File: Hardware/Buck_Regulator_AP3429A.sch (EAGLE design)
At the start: 8 parts

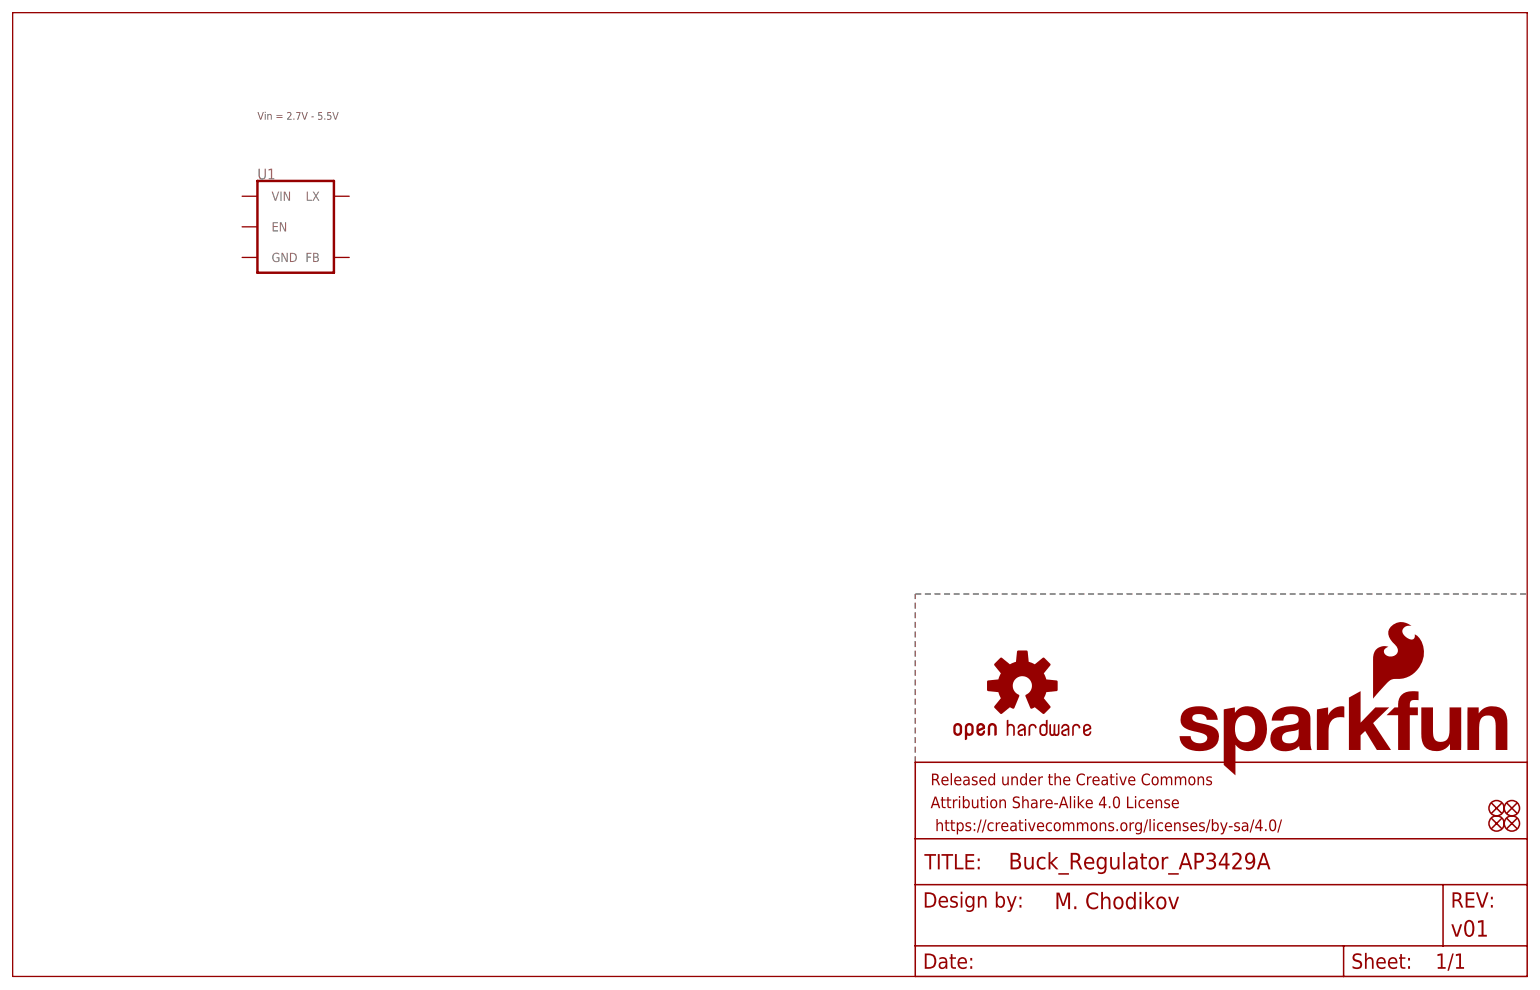
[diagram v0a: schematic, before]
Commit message: Addition of App Note, Updates to Schematic
Added connectors, power led, and main ic circuit with correctly rated components. The application note was added for the new product that Diodes Inc. sells, but it is the same exact part as the AP3429A but with a lower current limit (from 2A to 1A)
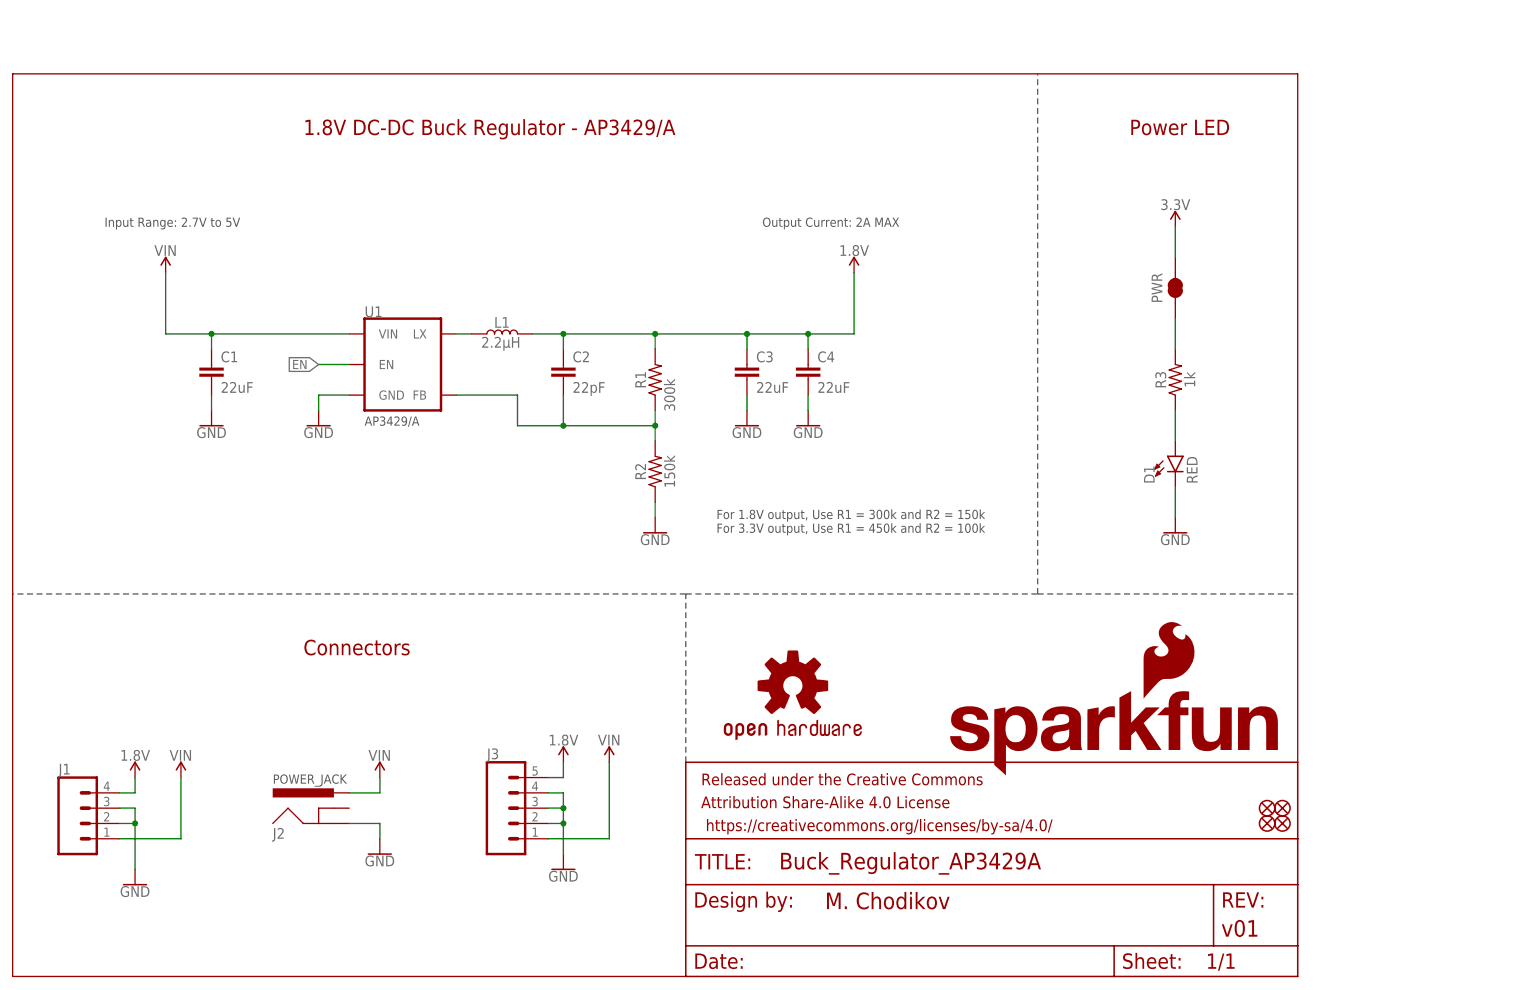
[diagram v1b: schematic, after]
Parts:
- added C1, C3, C4: 22uF, SparkFun-Capacitors:22UF-0603-6.3V-20%
- added C2: 22pF, SparkFun-Capacitors:22PF-0603-50V-5%
- added D1: RED, SparkFun-LED:LED-RED0603
- added J1: (no value), SparkFun-Connectors:CONN_04SCREW_LOCK
- added J2: POWER_JACKPOWER_JACK_SLOT, SparkFun-Connectors:POWER_JACKPOWER_JACK_SLOT
- added J3: (no value), SparkFun-Connectors:CONN_05
- added L1: 2.2μH, SparkFun-Coils:2.2μH-4X4-2.2μH-3A-45MOHM
- added PWR: JUMPER-SMT_2_NC_TRACE_SILK, SparkFun-Jumpers:JUMPER-SMT_2_NC_TRACE_SILK
- added R1: 300k, SparkFun-Resistors:300KOHM-0603-1/10W-1%
- added R2: 150k, SparkFun-Resistors:150KOHM-0603-1/10W-1%
- added R3: 1k, SparkFun-Resistors:1KOHM-0603-1/10W-1%
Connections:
- new net 1.8V: C2.1, C3.1, C4.1, J1.4, J3.5, L1.2, R1.2
- new net 3.3V: PWR.2
- new net EN: U1.EN
- new net GND: C1.2, C3.2, C4.2, D1.C, J2.GND, R2.1, U1.GND
- new net N$1: L1.1, U1.LX
- new net N$2: C2.2, R1.1, R2.2, U1.FB
- new net N$3: PWR.1, R3.2
- new net N$4: D1.A, R3.1
- new net N$6: J3.2, J3.3, J3.4
- new net N$7: J1.2, J1.3
- new net VIN: C1.1, J1.1, J2.PWR, J3.1, U1.VIN
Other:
- note added: "1.8V DC-DC Buck Regulator - AP3429/A"
- note added: "AP3429/A"
- note added: "Connectors"
- note added: "For 1.8V output, Use R1 = 300k and R2 = 150k For 3.3V output, Use R1 = 450k and R2 = 100k"
- note added: "Input Range: 2.7V to 5V"
- note added: "Output Current: 2A MAX"
- note added: "POWER_JACK"
- note added: "Power LED"
- note removed: "Vin = 2.7V - 5.5V"
- moved on the sheet: U1

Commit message: Update Buck_Regulator_AP3429A.sch
Attributes added for parts missing that information, finished first draft of initial schematic for 1.8V output, added further notation on what to change for 3.3V output instead of the 1.8V output.
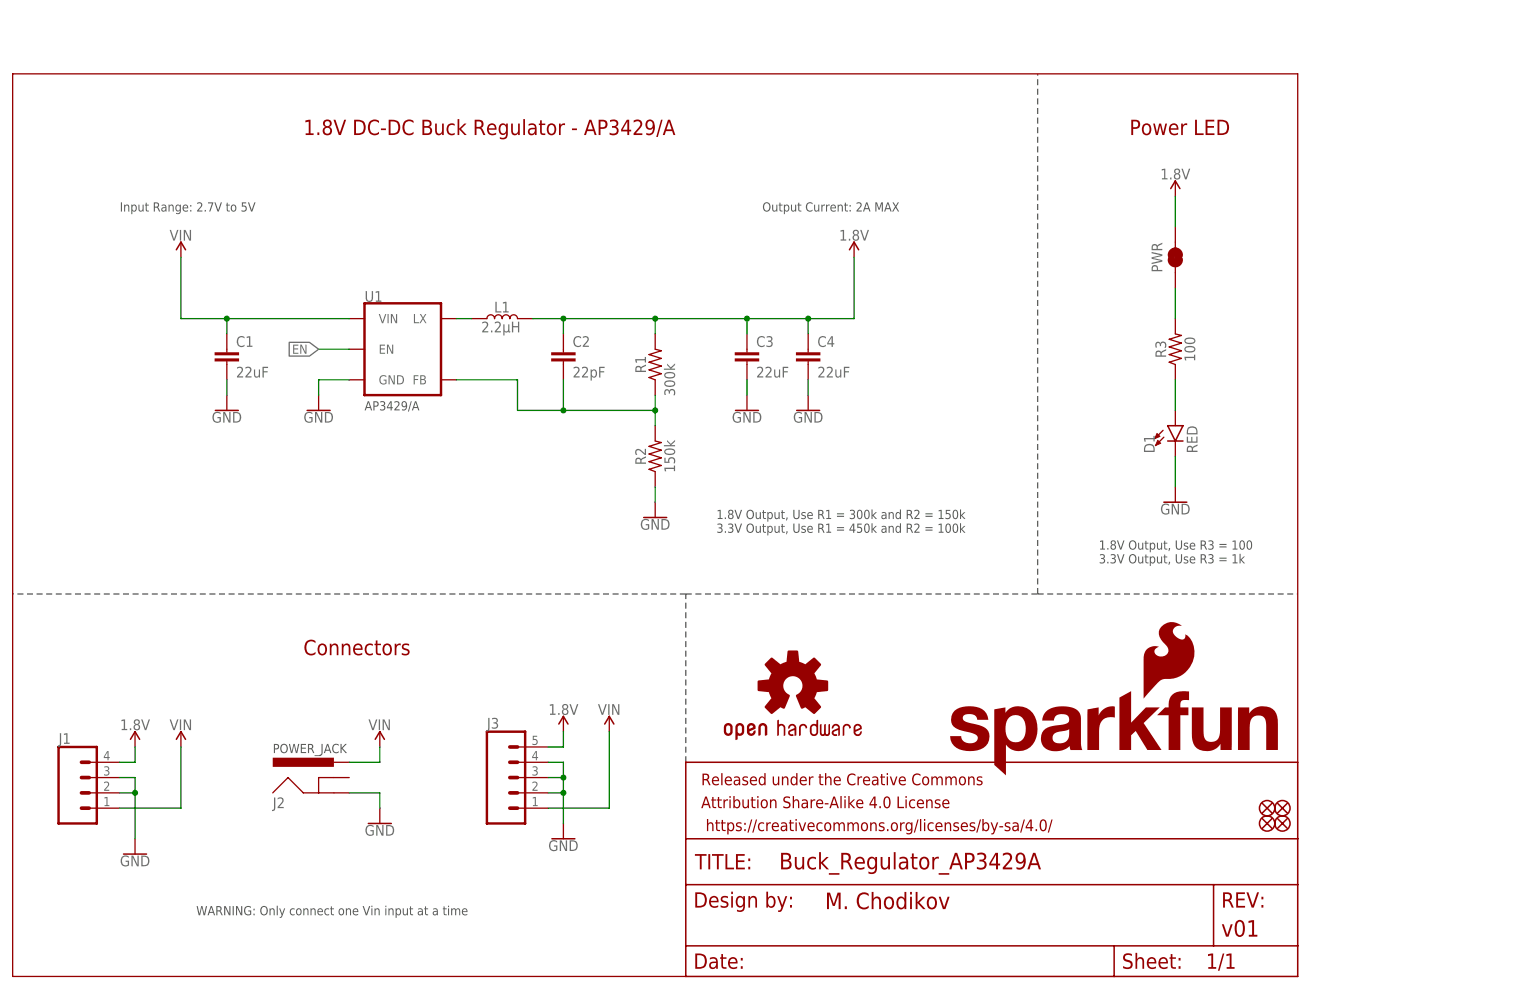
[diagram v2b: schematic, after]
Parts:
- C2: device SparkFun-Capacitors:22PF-0603-50V-5% -> SparkFun-Capacitors:22PF-0402T-16V-10%
- J1: PROD_ID (none) -> CONN-14485
- R3: value 1k -> 100; device SparkFun-Resistors:1KOHM-0603-1/10W-1% -> SparkFun-Resistors:100OHM-0603-1/10W-1%
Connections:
- removed net 3.3V: PWR.2
- net 1.8V: now also PWR.2
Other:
- note added: "1.8V Output, Use R1 = 300k and R2 = 150k 3.3V Output, Use R1 = 450k and R2 = 100k"
- note added: "1.8V Output, Use R3 = 100 3.3V Output, Use R3 = 1k"
- note added: "WARNING: Only connect one Vin input at a time"
- note removed: "For 1.8V output, Use R1 = 300k and R2 = 150k For 3.3V output, Use R1 = 450k and R2 = 100k"
- moved on the sheet: C1, C2, C3, C4, D1, J1, J2, J3, L1, PWR, R1, R2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

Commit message: Created Board file and cleaned up schematic
Added notation jumpers for 3.3V or 1.8V board, created board file and adjusted components to fit onto the board in a 1x1 form factor.
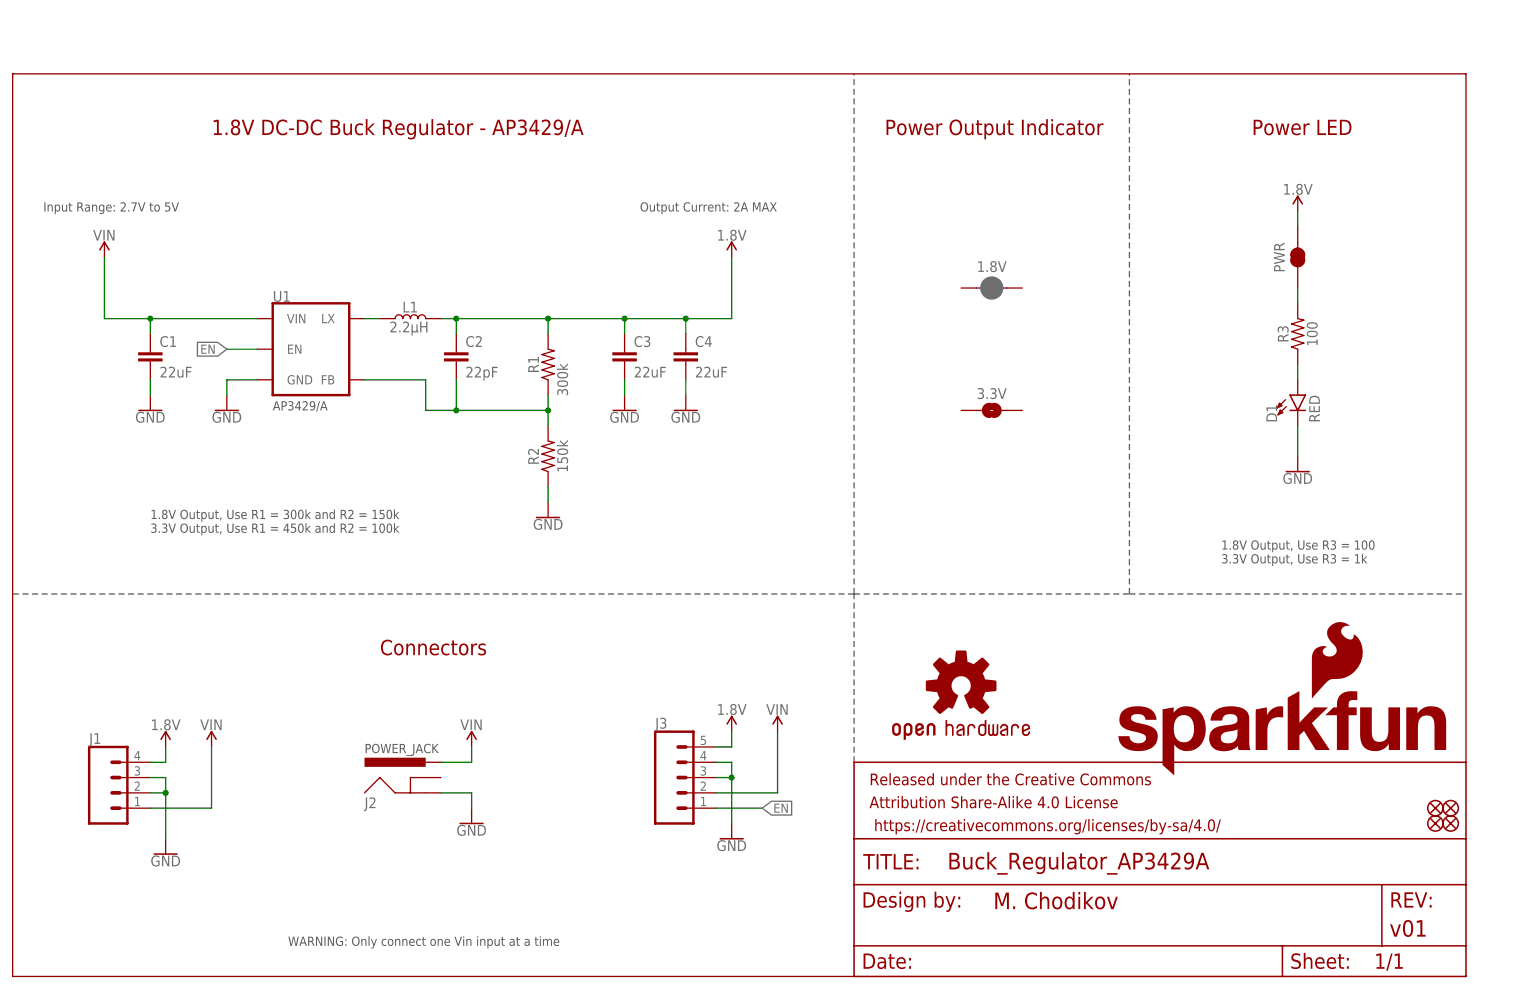
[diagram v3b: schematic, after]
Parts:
- added 1.8V: JUMPER-SMT_2_NC_PASTE_NO-SILK, SparkFun-Jumpers:JUMPER-SMT_2_NC_PASTE_NO-SILK
- added 3.3V: JUMPER-SMT_2_NO_NO-SILK, SparkFun-Jumpers:JUMPER-SMT_2_NO_NO-SILK
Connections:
- net EN: now also J3.1
- net N$6: no longer J3.2
- net VIN: now also J3.2; no longer J3.1
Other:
- note added: "Power Output Indicator"
- moved on the sheet: C1, C2, C3, C4, D1, J1, J2, J3, L1, PWR, R1, R2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

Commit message: Updates to project
Schematic: Changed indicator pads for soldering which version of board, added further notation, updated Power Jack device in local library.
Layout: Added power polygons and stitching vias to appropriate areas, finished routing, adjusted Power Jack to be double sided now, fixed silkscreen notation, adjusted version number, worked through design errors.
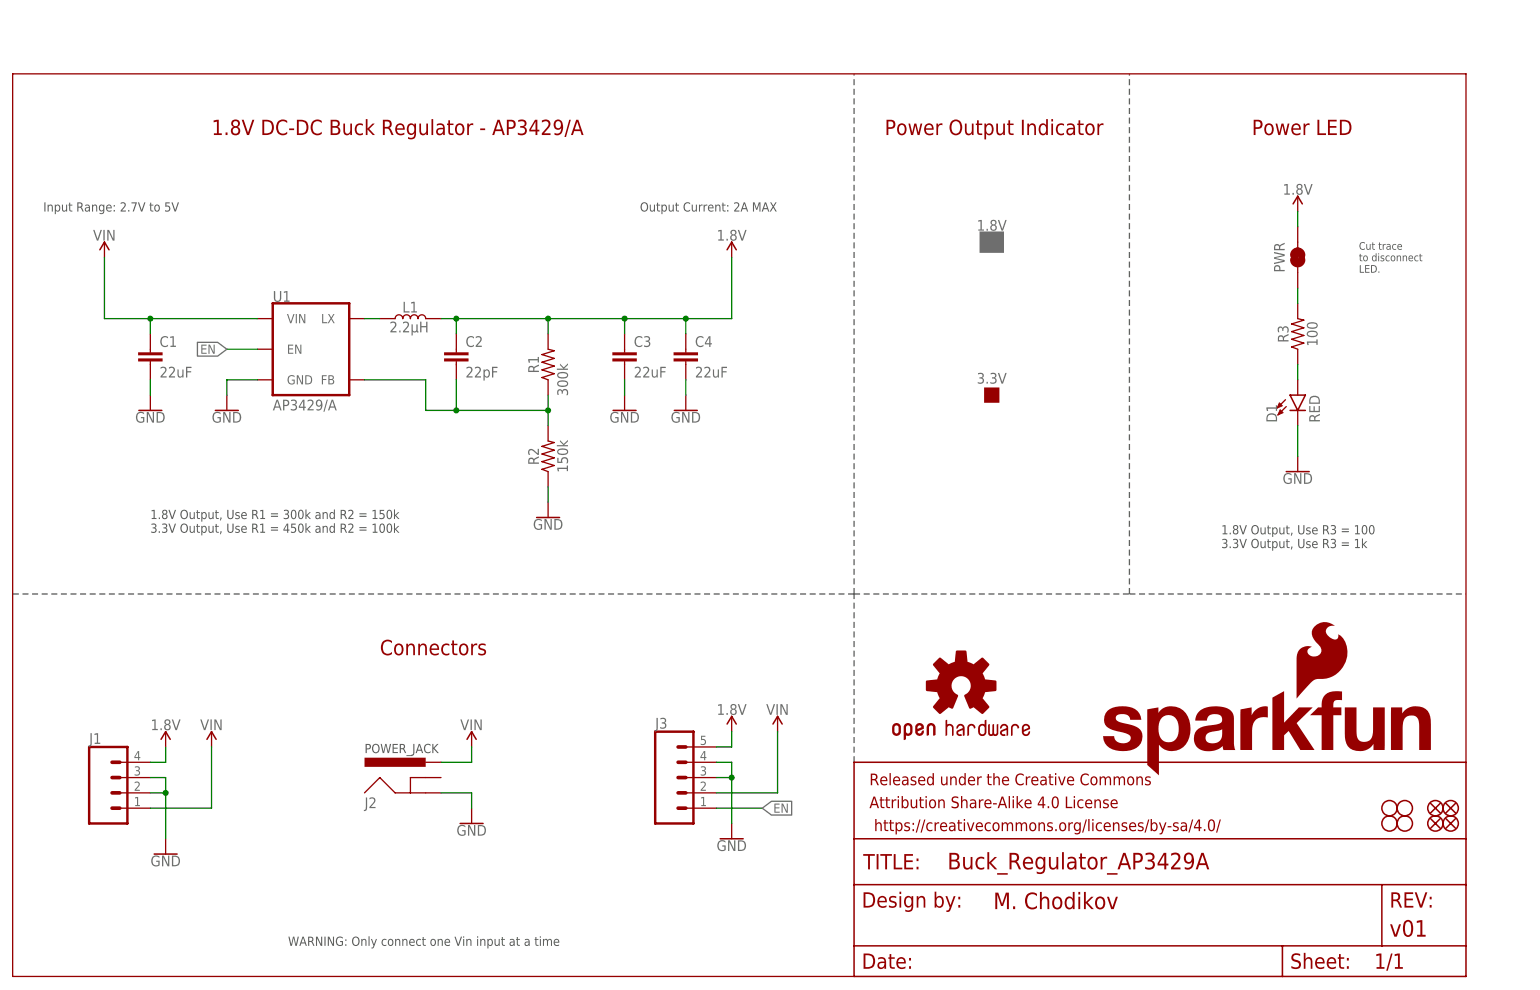
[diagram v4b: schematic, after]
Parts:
- added H1, H2, H3, H4: STAND-OFFTIGHT, SparkFun-Hardware:STAND-OFFTIGHT
- 1.8V: value JUMPER-SMT_2_NC_PASTE_NO-SILK -> PROD_ID_PASTE_NO-SILK; device SparkFun-Jumpers:JUMPER-SMT_2_NC_PASTE_NO-SILK -> SparkFun-Aesthetics:PROD_ID_PASTE_NO-SILK
- 3.3V: value JUMPER-SMT_2_NO_NO-SILK -> PROD_ID_NO-PASTE_NO_SILK; device SparkFun-Jumpers:JUMPER-SMT_2_NO_NO-SILK -> SparkFun-Aesthetics:PROD_ID_NO-PASTE_NO_SILK
- J1: value (none) -> Screw Terminal; device SparkFun-Connectors:CONN_04SCREW_LOCK -> SparkFun-Connectors:CONN_04SCREW; PROD_ID CONN-14485 -> (none)
- J2: value POWER_JACKPOWER_JACK_SLOT -> POWER_JACKPOWER_JACK_SLOT_COMBO; device SparkFun-Connectors:POWER_JACKPOWER_JACK_SLOT -> SparkFun-Connectors:POWER_JACKPOWER_JACK_SLOT_COMBO
- J3: value (none) -> Breakout Headers; device SparkFun-Connectors:CONN_05 -> SparkFun-Connectors:CONN_05NO_SILK
- LOGO1: value OSHW-LOGOM -> OSHW-LOGOS; device SparkFun-Aesthetics:OSHW-LOGOM -> SparkFun-Aesthetics:OSHW-LOGOS
- LOGO2: value SFE_LOGO_NAME_FLAME.2_INCH -> SFE_LOGO_NAME_FLAME.1_INCH; device SparkFun-Aesthetics:SFE_LOGO_NAME_FLAME.2_INCH -> SparkFun-Aesthetics:SFE_LOGO_NAME_FLAME.1_INCH
- U1: value (none) -> AP3429/A
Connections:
- removed net N$6: J3.3, J3.4
- removed net N$7: J1.2, J1.3
- net GND: now also J1.2, J1.3, J3.3, J3.4
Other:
- note added: "Cut trace to disconnect LED."
- note removed: "AP3429/A"

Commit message: heat sink addition - v01 design review
Changed the SparkFun logo on the backside of the board and separated the name and flame; added an area on the backside for the heatsink to be added; adjusted silkscreen and components on backside accordingly for heatsink; moved the EN trace to the topside of the board
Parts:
- added LOGO3: SFE_LOGO_FLAME.1_INCH, SparkFun-Aesthetics:SFE_LOGO_FLAME.1_INCH
- LOGO2: value SFE_LOGO_NAME_FLAME.1_INCH -> SFE_LOGO_NAME.1_INCH; device SparkFun-Aesthetics:SFE_LOGO_NAME_FLAME.1_INCH -> SparkFun-Aesthetics:SFE_LOGO_NAME.1_INCH
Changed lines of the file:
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@@
 <part name="H3" library="SparkFun-Hardware" deviceset="STAND-OFF" device="TIGHT"/>
 <part name="H4" library="SparkFun-Hardware" deviceset="STAND-OFF" device="TIGHT"/>
-<part name="LOGO2" library="SparkFun-Aesthetics" deviceset="SFE_LOGO_NAME_FLAME" device=".1_INCH"/>
 <part name="J3" library="SparkFun-Connectors" deviceset="CONN_05" device="NO_SILK" value="Breakout Headers"/>
 <part name="LOGO1" library="SparkFun-Aesthetics" deviceset="OSHW-LOGO" device="S"/>
@@
 <part name="1.8V" library="SparkFun-Aesthetics" deviceset="PROD_ID_PASTE" device="_NO-SILK"/>
 <part name="J2" library="SparkFun-Connectors" deviceset="POWER_JACK" device="POWER_JACK_SLOT_COMBO"/>
+<part name="LOGO3" library="SparkFun-Aesthetics" deviceset="SFE_LOGO_FLAME" device=".1_INCH"/>
+<part name="LOGO2" library="SparkFun-Aesthetics" deviceset="SFE_LOGO_NAME" device=".1_INCH"/>
 </parts>
 <sheets>
@@
 <instance part="H3" gate="G$1" x="228.6" y="25.4" smashed="yes"/>
 <instance part="H4" gate="G$1" x="231.14" y="25.4" smashed="yes"/>
-<instance part="LOGO2" gate="G$1" x="180.34" y="33.02" smashed="yes"/>
 <instance part="J3" gate="G$1" x="109.22" y="33.02" smashed="yes">
 <attribute name="NAME" x="106.68" y="41.148" size="1.778" layer="95" font="vector"/>
@@
 <attribute name="NAME" x="58.42" y="27.94" size="1.778" layer="95" font="vector"/>
 </instance>
+<instance part="LOGO3" gate="G$1" x="214.122" y="48.26" smashed="yes"/>
+<instance part="LOGO2" gate="G$1" x="180.34" y="35.56" smashed="yes"/>
 </instances>
 <busses>
